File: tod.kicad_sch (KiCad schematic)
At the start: 61 parts, among them J1 Conn_01x04, J2 Conn_01x03, J3 Conn_01x04, J4 Conn_01x03, Q1 BC856, Q2 BC817, Q3 BC856, Q4 BC817, Q5 BC856, Q6 BC817, Q7 BC856, Q8 BC817, U1 PC817, U2 PC817, U3 PC817, U4 PC817

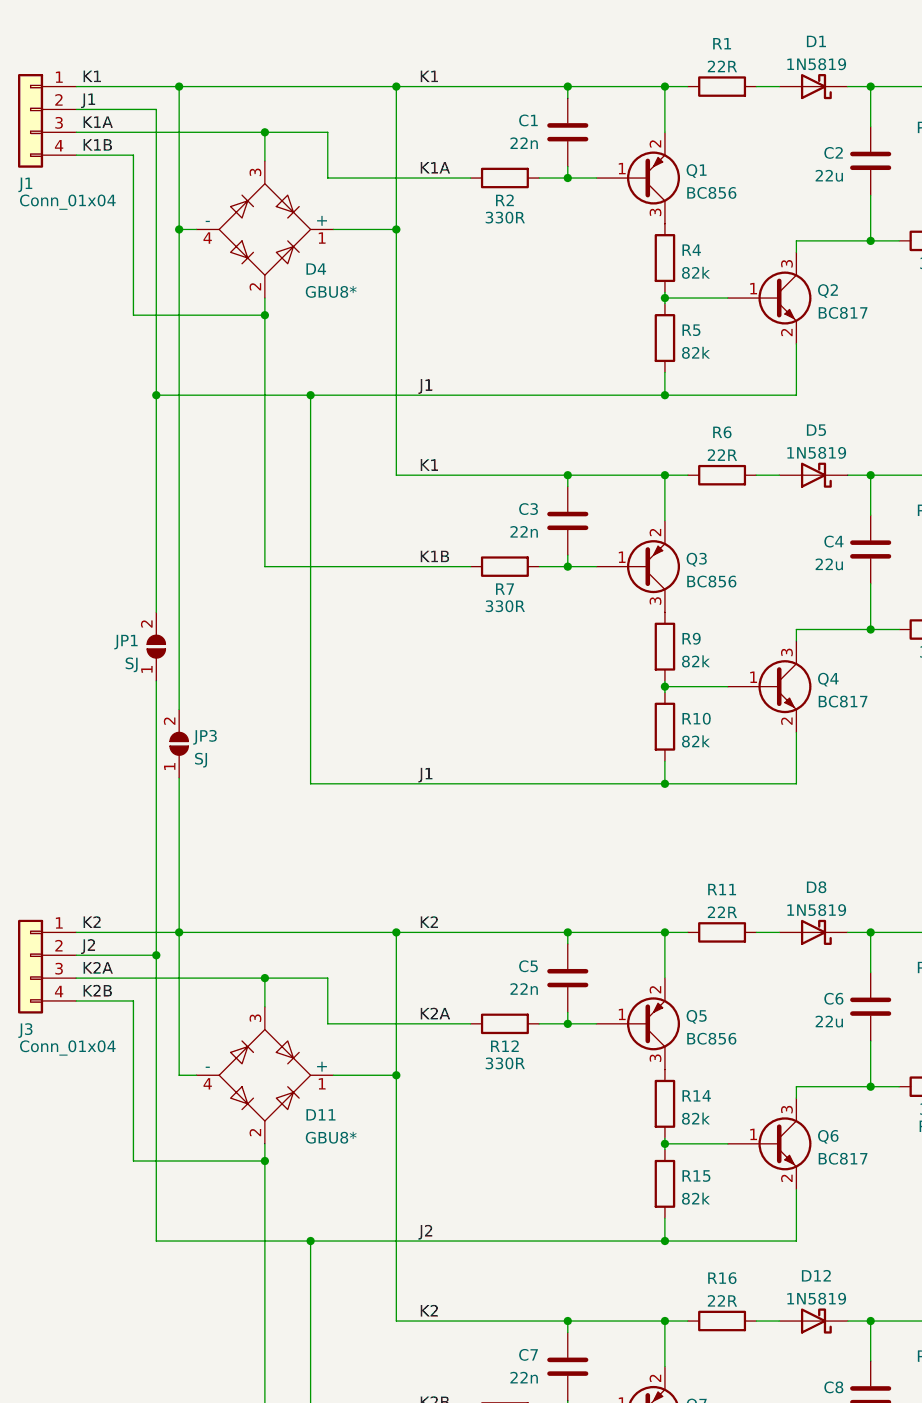
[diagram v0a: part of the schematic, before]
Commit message: Route PCB.
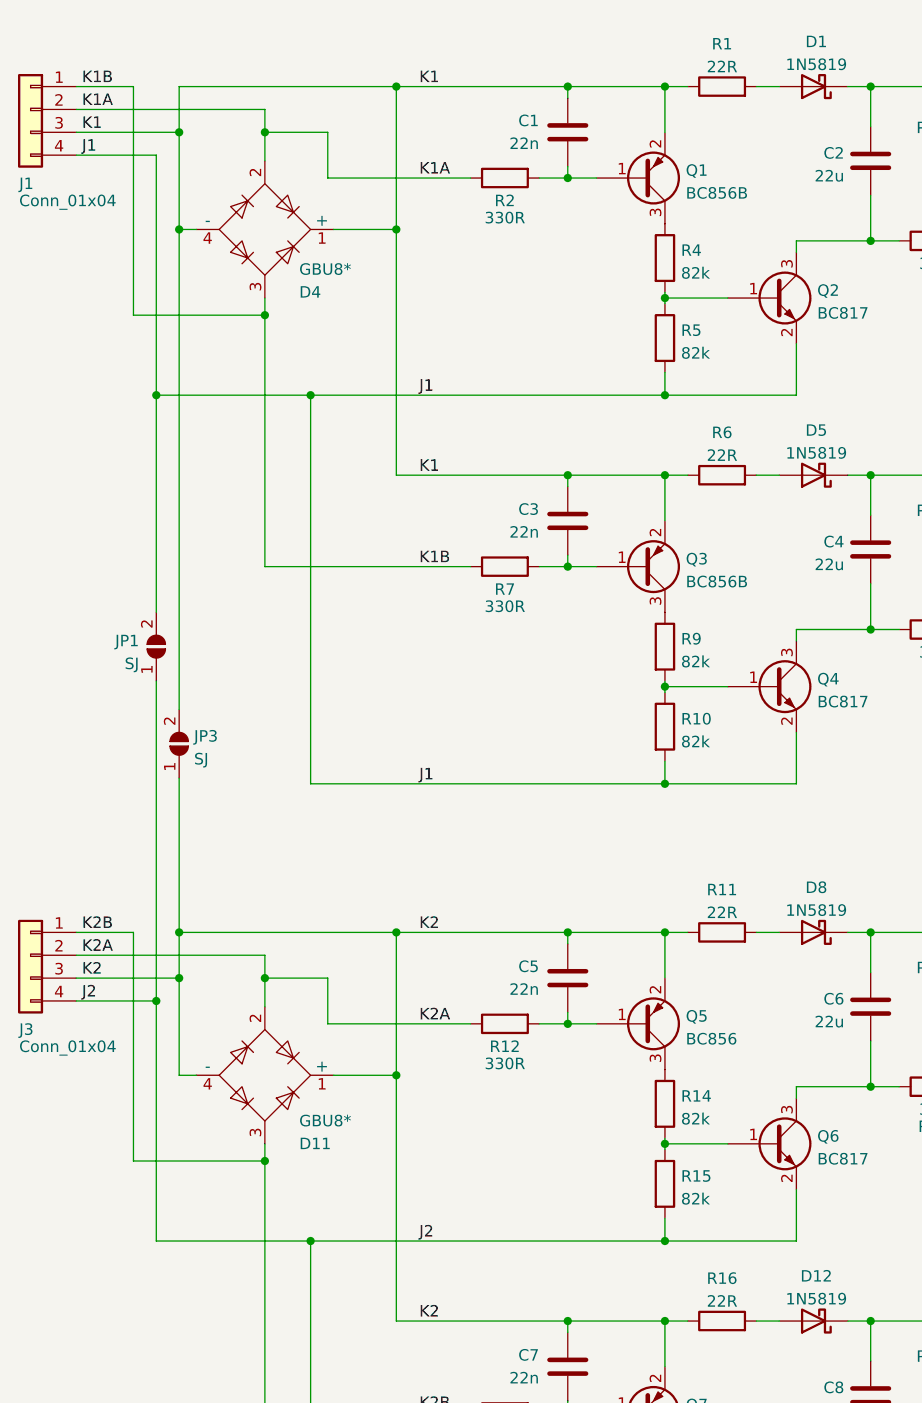
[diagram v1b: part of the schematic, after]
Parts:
- Q1, Q3: value BC856 -> BC856B; footprint Package_TO_SOT_SMD:SOT-23_Handsoldering -> Package_TO_SOT_SMD:SOT-23
- Q2, Q4, Q5, Q6, Q7, Q8: footprint Package_TO_SOT_SMD:SOT-23_Handsoldering -> Package_TO_SOT_SMD:SOT-23
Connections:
- net J1: now also J1.4 (Pin_4); no longer J1.2 (Pin_2)
- net J2: now also J3.4 (Pin_4); no longer J3.2 (Pin_2)
- net K1: now also J1.3 (Pin_3); no longer J1.1 (Pin_1)
- net K1A: now also D4.2, J1.2 (Pin_2); no longer D4.3, J1.3 (Pin_3)
- net K1B: now also D4.3, J1.1 (Pin_1); no longer D4.2, J1.4 (Pin_4)
- net K2: now also J3.3 (Pin_3); no longer J3.1 (Pin_1)
- net K2A: now also D11.2, J3.2 (Pin_2); no longer D11.3, J3.3 (Pin_3)
- net K2B: now also D11.3, J3.1 (Pin_1); no longer D11.2, J3.4 (Pin_4)

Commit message: Add proper MVE252-5-V footprints.
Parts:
- J1, J3: footprint TerminalBlock:TerminalBlock_Altech_AK300-4_P5.00mm -> TerminalBlock_Euroclamp:MVE252-5-V-2x
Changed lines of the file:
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@@
       (effects (font (size 1.27 1.27)) (justify right))
     )
-    (property "Footprint" "TerminalBlock:TerminalBlock_Altech_AK300-4_P5.00mm" (id 2) (at 23.495 118.11 0)
+    (property "Footprint" "TerminalBlock_Euroclamp:MVE252-5-V-2x" (id 2) (at 23.495 118.11 0)
       (effects (font (size 1.27 1.27)) hide)
     )
@@
       (effects (font (size 1.27 1.27)) (justify right))
     )
-    (property "Footprint" "TerminalBlock:TerminalBlock_Altech_AK300-4_P5.00mm" (id 2) (at 23.495 24.13 0)
+    (property "Footprint" "TerminalBlock_Euroclamp:MVE252-5-V-2x" (id 2) (at 23.495 24.13 0)
       (effects (font (size 1.27 1.27)) hide)
     )
@@
     )
     (path "/d0746bea-04cf-47f9-8742-bbc0cea547a0"
-      (reference "J1") (unit 1) (value "Conn_01x04") (footprint "TerminalBlock:TerminalBlock_Altech_AK300-4_P5.00mm")
+      (reference "J1") (unit 1) (value "Conn_01x04") (footprint "TerminalBlock_Euroclamp:MVE252-5-V-2x")
     )
     (path "/6caf5573-ee2b-4bb3-ae2c-0627f7e24055"
@@
     )
     (path "/80e68ac6-e437-4b3b-af1e-59dcd574c455"
-      (reference "J3") (unit 1) (value "Conn_01x04") (footprint "TerminalBlock:TerminalBlock_Altech_AK300-4_P5.00mm")
+      (reference "J3") (unit 1) (value "Conn_01x04") (footprint "TerminalBlock_Euroclamp:MVE252-5-V-2x")
     )
     (path "/80ba5ec6-7c03-4901-8dce-a7ca8c577c35"

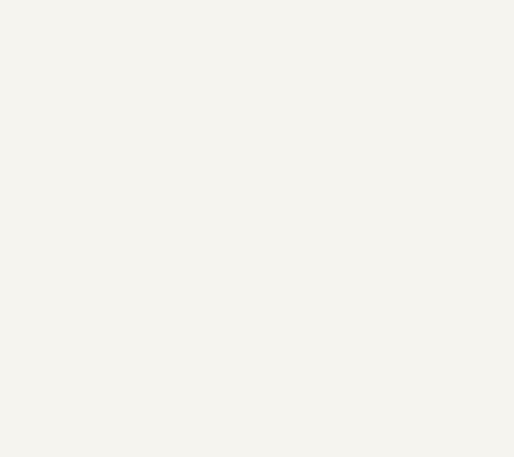
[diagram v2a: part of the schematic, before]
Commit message: Add mountholes.
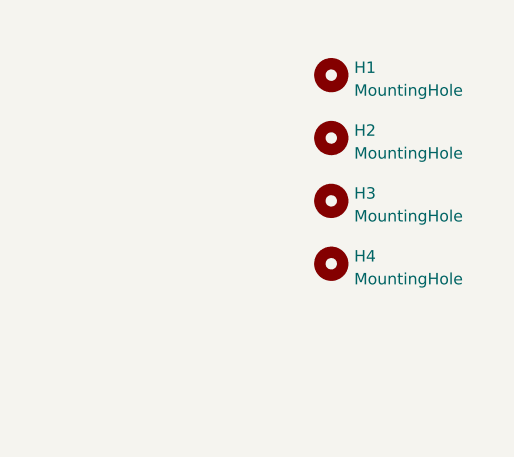
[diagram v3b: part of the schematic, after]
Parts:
- added H1, H2, H3, H4: MountingHole, MountingHole:MountingHole_3.2mm_M3_Pad, symbol Mechanical:MountingHole
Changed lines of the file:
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@@
     (pin "2")
+  )
+  (symbol (lib_id "Mechanical:MountingHole") (at 262.89 27.305 0) (unit 1)
+    (in_bom yes) (on_board yes) (fields_autoplaced)
+    (property "Reference" "H2" (id 0) (at 265.43 26.4703 0)
+      (effects (font (size 1.27 1.27)) (justify left))
+    )
+    (property "Value" "MountingHole" (id 1) (at 265.43 29.0072 0)
+      (effects (font (size 1.27 1.27)) (justify left))
+    )
+    (property "Footprint" "MountingHole:MountingHole_3.2mm_M3_Pad" (id 2) (at 262.89 27.305 0)
+      (effects (font (size 1.27 1.27)) hide)
+    )
+    (property "Datasheet" "~" (id 3) (at 262.89 27.305 0)
+      (effects (font (size 1.27 1.27)) hide)
+    )
   )
   (symbol (lib_id "Jumper:SolderJumper_2_Open") (at 156.845 92.075 90) (unit 1)
@@
     (pin "2")
   )
+  (symbol (lib_id "Mechanical:MountingHole") (at 262.89 20.32 0) (unit 1)
+    (in_bom yes) (on_board yes) (fields_autoplaced)
+    (property "Reference" "H1" (id 0) (at 265.43 19.4853 0)
+      (effects (font (size 1.27 1.27)) (justify left))
+    )
+    (property "Value" "MountingHole" (id 1) (at 265.43 22.0222 0)
+      (effects (font (size 1.27 1.27)) (justify left))
+    )
+    (property "Footprint" "MountingHole:MountingHole_3.2mm_M3_Pad" (id 2) (at 262.89 20.32 0)
+      (effects (font (size 1.27 1.27)) hide)
+    )
+    (property "Datasheet" "~" (id 3) (at 262.89 20.32 0)
+      (effects (font (size 1.27 1.27)) hide)
+    )
+  )
   (symbol (lib_id "Device:R") (at 100.33 64.77 90) (unit 1)
     (in_bom yes) (on_board yes) (fields_autoplaced)
@@
     (pin "2")
   )
+  (symbol (lib_id "Mechanical:MountingHole") (at 262.89 34.29 0) (unit 1)
+    (in_bom yes) (on_board yes) (fields_autoplaced)
+    (property "Reference" "H3" (id 0) (at 265.43 33.4553 0)
+      (effects (font (size 1.27 1.27)) (justify left))
+    )
+    (property "Value" "MountingHole" (id 1) (at 265.43 35.9922 0)
+      (effects (font (size 1.27 1.27)) (justify left))
+    )
+    (property "Footprint" "MountingHole:MountingHole_3.2mm_M3_Pad" (id 2) (at 262.89 34.29 0)
+      (effects (font (size 1.27 1.27)) hide)
+    )
+    (property "Datasheet" "~" (id 3) (at 262.89 34.29 0)
+      (effects (font (size 1.27 1.27)) hide)
+    )
+  )
   (symbol (lib_id "Device:LED") (at 136.525 125.73 90) (unit 1)
     (in_bom yes) (on_board yes)
@@
     (pin "2")
   )
+  (symbol (lib_id "Mechanical:MountingHole") (at 262.89 41.275 0) (unit 1)
+    (in_bom yes) (on_board yes) (fields_autoplaced)
+    (property "Reference" "H4" (id 0) (at 265.43 40.4403 0)
+      (effects (font (size 1.27 1.27)) (justify left))
+    )
+    (property "Value" "MountingHole" (id 1) (at 265.43 42.9772 0)
+      (effects (font (size 1.27 1.27)) (justify left))
+    )
+    (property "Footprint" "MountingHole:MountingHole_3.2mm_M3_Pad" (id 2) (at 262.89 41.275 0)
+      (effects (font (size 1.27 1.27)) hide)
+    )
+    (property "Datasheet" "~" (id 3) (at 262.89 41.275 0)
+      (effects (font (size 1.27 1.27)) hide)
+    )
+  )
   (symbol (lib_id "Device:R") (at 76.2 31.75 90) (mirror x) (unit 1)
     (in_bom yes) (on_board yes)
@@
       (reference "D14") (unit 1) (value "LED") (footprint "LED_THT:LED_D3.0mm")
     )
+    (path "/8bb13ebd-0f12-4a54-9b6c-3de65ff34af9"
+      (reference "H1") (unit 1) (value "MountingHole") (footprint "MountingHole:MountingHole_3.2mm_M3_Pad")
+    )
+    (path "/6dae2305-bf80-4b95-9d15-95773efe6150"
+      (reference "H2") (unit 1) (value "MountingHole") (footprint "MountingHole:MountingHole_3.2mm_M3_Pad")
+    )
+    (path "/e126d598-8ad3-4c3f-86a5-641c2ac0698e"
+      (reference "H3") (unit 1) (value "MountingHole") (footprint "MountingHole:MountingHole_3.2mm_M3_Pad")
+    )
+    (path "/fabc5b30-6e01-48d8-b81c-b27d7b1c606f"
+      (reference "H4") (unit 1) (value "MountingHole") (footprint "MountingHole:MountingHole_3.2mm_M3_Pad")
+    )
     (path "/d0746bea-04cf-47f9-8742-bbc0cea547a0"

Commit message: Add kikit fab process.
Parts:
- D10, D11, D14, D2, D4, D7, J1, J2, J3, J4, U1, U2, U3, U4: JLCPCB_IGNORE (none) -> -
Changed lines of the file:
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@@
       (effects (font (size 1.27 1.27)) (justify left) hide)
+    )
+    (property "JLCPCB_IGNORE" "-" (id 4) (at 146.05 161.29 0)
+      (effects (font (size 1.27 1.27)) hide)
     )
     (pin "1")
@@
       (effects (font (size 1.27 1.27)) (justify left) hide)
     )
+    (property "JLCPCB_IGNORE" "-" (id 4) (at 146.05 24.13 0)
+      (effects (font (size 1.27 1.27)) hide)
+    )
     (pin "1")
     (pin "2")
@@
       (effects (font (size 1.27 1.27)) hide)
     )
+    (property "JLCPCB_IGNORE" "-" (id 4) (at 136.525 74.93 90)
+      (effects (font (size 1.27 1.27)) hide)
+    )
     (pin "1")
     (pin "2")
@@
       (effects (font (size 1.27 1.27)) hide)
     )
+    (property "JLCPCB_IGNORE" "-" (id 4) (at 176.53 24.13 0)
+      (effects (font (size 1.27 1.27)) hide)
+    )
     (pin "1")
     (pin "2")
@@
       (effects (font (size 1.27 1.27)) hide)
     )
+    (property "JLCPCB_IGNORE" "-" (id 4) (at 176.53 118.11 0)
+      (effects (font (size 1.27 1.27)) hide)
+    )
     (pin "1")
     (pin "2")
@@
     )
     (property "Datasheet" "~" (id 3) (at 23.495 118.11 0)
+      (effects (font (size 1.27 1.27)) hide)
+    )
+    (property "JLCPCB_IGNORE" "-" (id 4) (at 23.495 118.11 0)
       (effects (font (size 1.27 1.27)) hide)
     )
@@
       (effects (font (size 1.27 1.27)) (justify left) hide)
     )
+    (property "JLCPCB_IGNORE" "-" (id 4) (at 146.05 67.31 0)
+      (effects (font (size 1.27 1.27)) hide)
+    )
     (pin "1")
     (pin "2")
@@
       (effects (font (size 1.27 1.27)) (justify left) hide)
     )
+    (property "JLCPCB_IGNORE" "-" (id 4) (at 146.05 118.11 0)
+      (effects (font (size 1.27 1.27)) hide)
+    )
     (pin "1")
     (pin "2")
@@
       (effects (font (size 1.27 1.27)) hide)
     )
+    (property "JLCPCB_IGNORE" "-" (id 4) (at 23.495 24.13 0)
+      (effects (font (size 1.27 1.27)) hide)
+    )
     (pin "1")
     (pin "2")
@@
       (effects (font (size 1.27 1.27)) hide)
     )
+    (property "JLCPCB_IGNORE" "-" (id 4) (at 49.53 131.445 0)
+      (effects (font (size 1.27 1.27)) hide)
+    )
     (pin "1")
     (pin "2")
@@
       (effects (font (size 1.27 1.27)) hide)
     )
+    (property "JLCPCB_IGNORE" "-" (id 4) (at 49.53 37.465 0)
+      (effects (font (size 1.27 1.27)) hide)
+    )
     (pin "1")
     (pin "2")
@@
     )
     (property "Datasheet" "~" (id 3) (at 136.525 125.73 0)
+      (effects (font (size 1.27 1.27)) hide)
+    )
+    (property "JLCPCB_IGNORE" "-" (id 4) (at 136.525 125.73 90)
       (effects (font (size 1.27 1.27)) hide)
     )
@@
       (effects (font (size 1.27 1.27)) hide)
     )
+    (property "JLCPCB_IGNORE" "-" (id 4) (at 136.525 168.91 90)
+      (effects (font (size 1.27 1.27)) hide)
+    )
     (pin "1")
     (pin "2")
@@
       (effects (font (size 1.27 1.27)) hide)
     )
+    (property "JLCPCB_IGNORE" "-" (id 4) (at 136.525 31.75 90)
+      (effects (font (size 1.27 1.27)) hide)
+    )

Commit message: Add JLCPCB_CORRECTION where required.
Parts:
- Q2, Q4, Q6, Q8: JLCPCB_CORRECTION (none) -> 0;0;180
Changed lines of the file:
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@@
+      (effects (font (size 1.27 1.27)) hide)
+    )
+    (property "JLCPCB_CORRECTION" "0;0;180" (id 5) (at 106.045 88.265 0)
       (effects (font (size 1.27 1.27)) hide)
     )
@@
       (effects (font (size 1.27 1.27)) hide)
     )
+    (property "JLCPCB_CORRECTION" "0;0;180" (id 5) (at 106.045 45.085 0)
+      (effects (font (size 1.27 1.27)) hide)
+    )
     (pin "1")
     (pin "2")
@@
       (effects (font (size 1.27 1.27)) hide)
     )
+    (property "JLCPCB_CORRECTION" "0;0;180" (id 5) (at 106.045 182.245 0)
+      (effects (font (size 1.27 1.27)) hide)
+    )
     (pin "1")
     (pin "2")
@@
       (effects (font (size 1.27 1.27)) hide)
     )
+    (property "JLCPCB_CORRECTION" "0;0;180" (id 5) (at 106.045 139.065 0)
+      (effects (font (size 1.27 1.27)) hide)
+    )

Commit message: LCSC: use cheaper transistors than BC817.
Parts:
- Q2, Q4, Q6, Q8: LCSC C52801 -> C2150
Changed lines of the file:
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@@
       (effects (font (size 1.27 1.27)) (justify left) hide)
     )
-    (property "LCSC" "C52801" (id 4) (at 106.045 88.265 0)
+    (property "LCSC" "C2150" (id 4) (at 106.045 88.265 0)
       (effects (font (size 1.27 1.27)) hide)
     )
@@
       (effects (font (size 1.27 1.27)) (justify left) hide)
     )
-    (property "LCSC" "C52801" (id 4) (at 106.045 45.085 0)
+    (property "LCSC" "C2150" (id 4) (at 106.045 45.085 0)
       (effects (font (size 1.27 1.27)) hide)
     )
@@
       (effects (font (size 1.27 1.27)) (justify left) hide)
     )
-    (property "LCSC" "C52801" (id 4) (at 106.045 182.245 0)
+    (property "LCSC" "C2150" (id 4) (at 106.045 182.245 0)
       (effects (font (size 1.27 1.27)) hide)
     )
@@
       (effects (font (size 1.27 1.27)) (justify left) hide)
     )
-    (property "LCSC" "C52801" (id 4) (at 106.045 139.065 0)
-      (effects (font (size 1.27 1.27)) hide)
-    )
+    (property "LCSC" "C2150" (id 4) (at 106.045 139.065 0)
+      (effects (font (size 1.27 1.27)) hide)
+    )

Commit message: Use cheaper transistors.
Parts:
- Q1, Q3, Q5, Q7: LCSC C2926215 -> C2149
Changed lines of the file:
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@@
       (effects (font (size 1.27 1.27)) (justify left) hide)
     )
-    (property "LCSC" "C2926215" (id 4) (at 91.44 125.73 0)
+    (property "LCSC" "C2149" (id 4) (at 91.44 125.73 0)
       (effects (font (size 1.27 1.27)) hide)
     )
@@
       (effects (font (size 1.27 1.27)) (justify left) hide)
     )
-    (property "LCSC" "C2926215" (id 4) (at 91.44 31.75 0)
+    (property "LCSC" "C2149" (id 4) (at 91.44 31.75 0)
       (effects (font (size 1.27 1.27)) hide)
     )
@@
       (effects (font (size 1.27 1.27)) (justify left) hide)
     )
-    (property "LCSC" "C2926215" (id 4) (at 91.44 168.91 0)
+    (property "LCSC" "C2149" (id 4) (at 91.44 168.91 0)
       (effects (font (size 1.27 1.27)) hide)
     )
@@
       (effects (font (size 1.27 1.27)) (justify left) hide)
     )
-    (property "LCSC" "C2926215" (id 4) (at 91.44 74.93 0)
-      (effects (font (size 1.27 1.27)) hide)
-    )
+    (property "LCSC" "C2149" (id 4) (at 91.44 74.93 0)
+      (effects (font (size 1.27 1.27)) hide)
+    )

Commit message: Do not place non-necessarry diodes.
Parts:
- D13, D3, D6, D9: JLCPCB_IGNORE (none) -> -
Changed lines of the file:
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@@
+      (effects (font (size 1.27 1.27)) hide)
+    )
+    (property "JLCPCB_IGNORE" "-" (id 5) (at 131.445 125.73 90)
       (effects (font (size 1.27 1.27)) hide)
     )
@@
     )
     (property "LCSC" "C191023" (id 4) (at 131.445 74.93 0)
+      (effects (font (size 1.27 1.27)) hide)
+    )
+    (property "JLCPCB_IGNORE" "-" (id 5) (at 131.445 74.93 90)
       (effects (font (size 1.27 1.27)) hide)
     )
@@
     )
     (property "LCSC" "C191023" (id 4) (at 131.445 32.385 0)
+      (effects (font (size 1.27 1.27)) hide)
+    )
+    (property "JLCPCB_IGNORE" "-" (id 5) (at 131.445 32.385 90)
       (effects (font (size 1.27 1.27)) hide)
     )
@@
       (effects (font (size 1.27 1.27)) hide)
     )
+    (property "JLCPCB_IGNORE" "-" (id 5) (at 131.445 168.91 90)
+      (effects (font (size 1.27 1.27)) hide)
+    )
